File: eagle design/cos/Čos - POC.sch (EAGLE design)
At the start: 117 parts, among them IC1 SQJ952EP-T1_GE3, IC10 LM74670QDGKRQ1, IC11 LM74670QDGKRQ1, IC12 LM74670QDGKRQ1, IC13 MCP73871-2CCI/ML, IC14 MCP2515, IC15 LM74670QDGKRQ1, IC16 LM74670QDGKRQ1, IC17 MCP23S08-E/ML, IC18 MCP2561-2, IC19 AD5160BRJZ5-R2, IC2 SQJ952EP-T1_GE3, IC20 MP3221GJ-P, IC21 SQJ952EP-T1_GE3, IC22 LM74670QDGKRQ1, IC23 SQJ952EP-T1_GE3, IC3 LM74670QDGKRQ1, IC4 SQJ952EP-T1_GE3, IC5 FDMQ8403, IC6 TPS630702RNMT, IC7 LMP92064SD/NOPB, IC8 ATTINY4313-MMH, IC9 PBRC8.00GR50X000

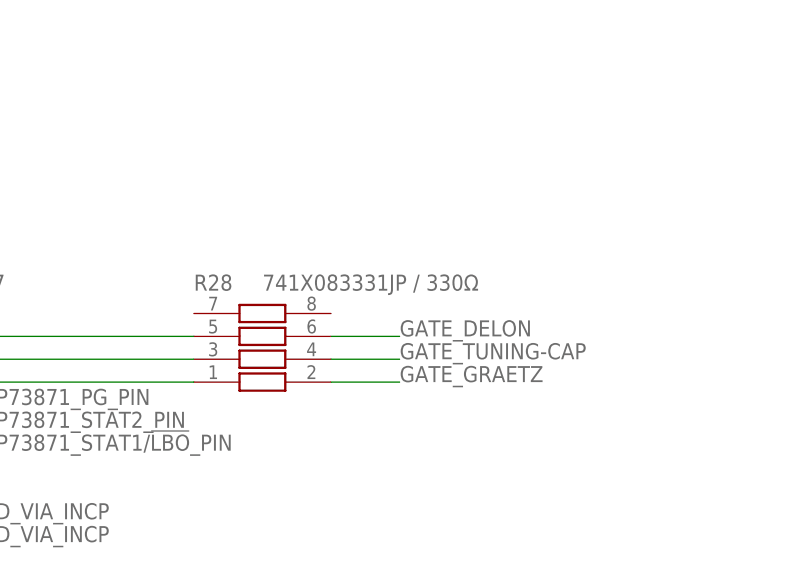
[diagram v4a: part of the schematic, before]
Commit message: - added series resistor for gate pins
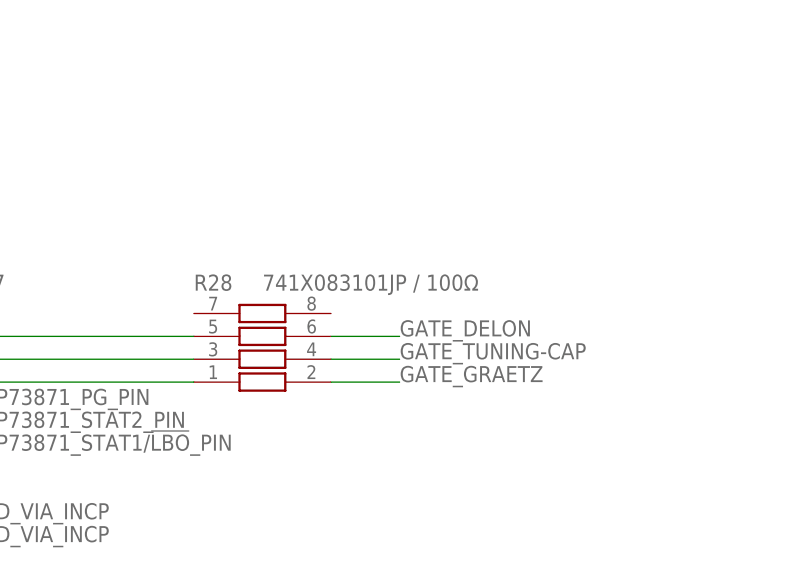
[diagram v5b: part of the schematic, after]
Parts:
- R28: value 741X083331JP / 330Ω -> 741X083101JP / 100Ω
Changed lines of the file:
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@@
 <grid distance="0.1" unitdist="inch" unit="inch" style="lines" multiple="1" display="no" altdistance="0.01" altunitdist="inch" altunit="inch"/>
 <layers>
-<layer number="1" name="Top" color="4" fill="1" visible="yes" active="no"/>
-<layer number="2" name="Route2" color="26" fill="1" visible="yes" active="no"/>
-<layer number="3" name="Route3" color="4" fill="3" visible="yes" active="no"/>
-<layer number="4" name="Route4" color="1" fill="4" visible="yes" active="no"/>
-<layer number="5" name="Route5" color="4" fill="4" visible="yes" active="no"/>
-<layer number="6" name="Route6" color="1" fill="8" visible="yes" active="no"/>
-<layer number="7" name="Route7" color="4" fill="8" visible="yes" active="no"/>
-<layer number="8" name="Route8" color="1" fill="2" visible="yes" active="no"/>
-<layer number="9" name="Route9" color="4" fill="2" visible="yes" active="no"/>
-<layer number="10" name="Route10" color="1" fill="7" visible="yes" active="no"/>
-<layer number="11" name="Route11" color="4" fill="7" visible="yes" active="no"/>
-<layer number="12" name="Route12" color="1" fill="5" visible="yes" active="no"/>
-<layer number="13" name="Route13" color="4" fill="5" visible="yes" active="no"/>
-<layer number="14" name="Route14" color="1" fill="6" visible="yes" active="no"/>
-<layer number="15" name="Route15" color="24" fill="1" visible="yes" active="no"/>
-<layer number="16" name="Bottom" color="1" fill="1" visible="yes" active="no"/>
-<layer number="17" name="Pads" color="2" fill="1" visible="yes" active="no"/>
-<layer number="18" name="Vias" color="2" fill="1" visible="yes" active="no"/>
-<layer number="19" name="Unrouted" color="6" fill="1" visible="yes" active="no"/>
-<layer number="20" name="Dimension" color="24" fill="1" visible="yes" active="no"/>
-<layer number="21" name="tPlace" color="7" fill="1" visible="yes" active="no"/>
-<layer number="22" name="bPlace" color="7" fill="1" visible="yes" active="no"/>
-<layer number="23" name="tOrigins" color="15" fill="1" visible="yes" active="no"/>
-<layer number="24" name="bOrigins" color="15" fill="1" visible="yes" active="no"/>
-<layer number="25" name="tNames" color="7" fill="1" visible="yes" active="no"/>
-<layer number="26" name="bNames" color="7" fill="1" visible="yes" active="no"/>
-<layer number="27" name="tValues" color="7" fill="1" visible="yes" active="no"/>
-<layer number="28" name="bValues" color="7" fill="1" visible="yes" active="no"/>
+<layer number="1" name="Top" color="4" fill="1" visible="no" active="no"/>
+<layer number="2" name="Route2" color="26" fill="1" visible="no" active="no"/>
+<layer number="3" name="Route3" color="4" fill="3" visible="no" active="no"/>
+<layer number="4" name="Route4" color="1" fill="4" visible="no" active="no"/>
+<layer number="5" name="Route5" color="4" fill="4" visible="no" active="no"/>
+<layer number="6" name="Route6" color="1" fill="8" visible="no" active="no"/>
+<layer number="7" name="Route7" color="4" fill="8" visible="no" active="no"/>
+<layer number="8" name="Route8" color="1" fill="2" visible="no" active="no"/>
+<layer number="9" name="Route9" color="4" fill="2" visible="no" active="no"/>
+<layer number="10" name="Route10" color="1" fill="7" visible="no" active="no"/>
+<layer number="11" name="Route11" color="4" fill="7" visible="no" active="no"/>
+<layer number="12" name="Route12" color="1" fill="5" visible="no" active="no"/>
+<layer number="13" name="Route13" color="4" fill="5" visible="no" active="no"/>
+<layer number="14" name="Route14" color="1" fill="6" visible="no" active="no"/>
+<layer number="15" name="Route15" color="24" fill="1" visible="no" active="no"/>
+<layer number="16" name="Bottom" color="1" fill="1" visible="no" active="no"/>
+<layer number="17" name="Pads" color="2" fill="1" visible="no" active="no"/>
+<layer number="18" name="Vias" color="2" fill="1" visible="no" active="no"/>
+<layer number="19" name="Unrouted" color="6" fill="1" visible="no" active="no"/>
+<layer number="20" name="Dimension" color="24" fill="1" visible="no" active="no"/>
+<layer number="21" name="tPlace" color="7" fill="1" visible="no" active="no"/>
+<layer number="22" name="bPlace" color="7" fill="1" visible="no" active="no"/>
+<layer number="23" name="tOrigins" color="15" fill="1" visible="no" active="no"/>
+<layer number="24" name="bOrigins" color="15" fill="1" visible="no" active="no"/>
+<layer number="25" name="tNames" color="7" fill="1" visible="no" active="no"/>
+<layer number="26" name="bNames" color="7" fill="1" visible="no" active="no"/>
+<layer number="27" name="tValues" color="7" fill="1" visible="no" active="no"/>
+<layer number="28" name="bValues" color="7" fill="1" visible="no" active="no"/>
 <layer number="29" name="tStop" color="7" fill="3" visible="no" active="no"/>
 <layer number="30" name="bStop" color="7" fill="6" visible="no" active="no"/>
@@
 <layer number="35" name="tGlue" color="7" fill="4" visible="no" active="no"/>
 <layer number="36" name="bGlue" color="7" fill="5" visible="no" active="no"/>
-<layer number="37" name="tTest" color="7" fill="1" visible="yes" active="no"/>
-<layer number="38" name="bTest" color="7" fill="1" visible="yes" active="no"/>
+<layer number="37" name="tTest" color="7" fill="1" visible="no" active="no"/>
+<layer number="38" name="bTest" color="7" fill="1" visible="no" active="no"/>
 <layer number="39" name="tKeepout" color="4" fill="11" visible="no" active="no"/>
 <layer number="40" name="bKeepout" color="1" fill="11" visible="no" active="no"/>
@@
 <layer number="44" name="Drills" color="7" fill="1" visible="no" active="no"/>
 <layer number="45" name="Holes" color="7" fill="1" visible="no" active="no"/>
-<layer number="46" name="Milling" color="3" fill="1" visible="yes" active="no"/>
-<layer number="47" name="Measures" color="7" fill="1" visible="yes" active="no"/>
-<layer number="48" name="Document" color="7" fill="1" visible="yes" active="no"/>
-<layer number="49" name="Reference" color="7" fill="1" visible="yes" active="no"/>
-<layer number="50" name="dxf" color="7" fill="1" visible="yes" active="no"/>
-<layer number="51" name="tDocu" color="7" fill="1" visible="yes" active="no"/>
-<layer number="52" name="bDocu" color="7" fill="1" visible="yes" active="no"/>
-<layer number="53" name="tGND_GNDA" color="7" fill="9" visible="yes" active="no"/>
-<layer number="54" name="bGND_GNDA" color="1" fill="9" visible="yes" active="no"/>
-<layer number="56" name="wert" color="7" fill="1" visible="yes" active="no"/>
-<layer number="57" name="tCAD" color="7" fill="1" visible="yes" active="no"/>
-<layer number="59" name="tCarbon" color="7" fill="1" visible="yes" active="no"/>
-<layer number="60" name="bCarbon" color="7" fill="1" visible="yes" active="no"/>
+<layer number="46" name="Milling" color="3" fill="1" visible="no" active="no"/>
+<layer number="47" name="Measures" color="7" fill="1" visible="no" active="no"/>
+<layer number="48" name="Document" color="7" fill="1" visible="no" active="no"/>
+<layer number="49" name="Reference" color="7" fill="1" visible="no" active="no"/>
+<layer number="50" name="dxf" color="7" fill="1" visible="no" active="no"/>
+<layer number="51" name="tDocu" color="7" fill="1" visible="no" active="no"/>
+<layer number="52" name="bDocu" color="7" fill="1" visible="no" active="no"/>
+<layer number="53" name="tGND_GNDA" color="7" fill="9" visible="no" active="no"/>
+<layer number="54" name="bGND_GNDA" color="1" fill="9" visible="no" active="no"/>
+<layer number="56" name="wert" color="7" fill="1" visible="no" active="no"/>
+<layer number="57" name="tCAD" color="7" fill="1" visible="no" active="no"/>
+<layer number="59" name="tCarbon" color="7" fill="1" visible="no" active="no"/>
+<layer number="60" name="bCarbon" color="7" fill="1" visible="no" active="no"/>
 <layer number="88" name="SimResults" color="9" fill="1" visible="yes" active="yes"/>
 <layer number="89" name="SimProbes" color="9" fill="1" visible="yes" active="yes"/>
@@
 <part name="FD2" library="Fiducial" deviceset="FID" device="_40MIL"/>
 <part name="FD3" library="Fiducial" deviceset="FID" device="_40MIL"/>
-<part name="R28" library="741X083331JP Resistor Array" deviceset="741X083331JP" device="" value="741X083331JP / 330Ω"/>
+<part name="R28" library="741X083331JP Resistor Array" deviceset="741X083331JP" device="" value="741X083101JP  / 100Ω"/>
 </parts>
 <sheets>

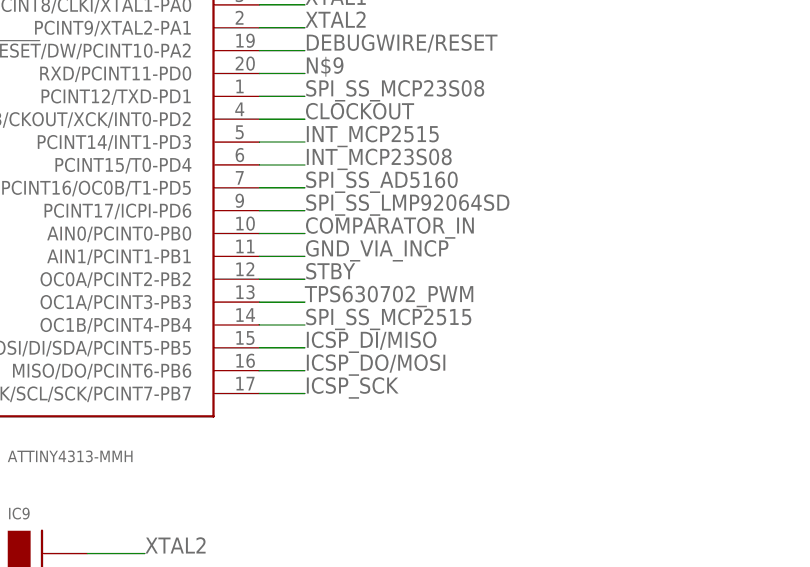
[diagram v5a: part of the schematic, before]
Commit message: in sch and brd: - pin swapped STBY and buck-boost PWM pins so that the comparator can work with timer1; buck-boost PWM is only 8bit
in cos.c and .h:
- configured comparator pins
- configured comparator to trigger on rising edge and enabled timer1 input capture function,
- configured timer1 for input capture, noise canceler, capture on rising edge, TOP = ICR1
- configured ICIE1 (Input Capture) and TOIE1 (timer overflow) interrupts
- enabled pin change interrupts for INT_MCP23S08_pin - PD4,
- wrote skeleton TIMER1_CAPT_vect and TIMER1_OVF_vect ISRs
- OCR_BUCK_BOOST holds PWM for Buck/Boost regulator
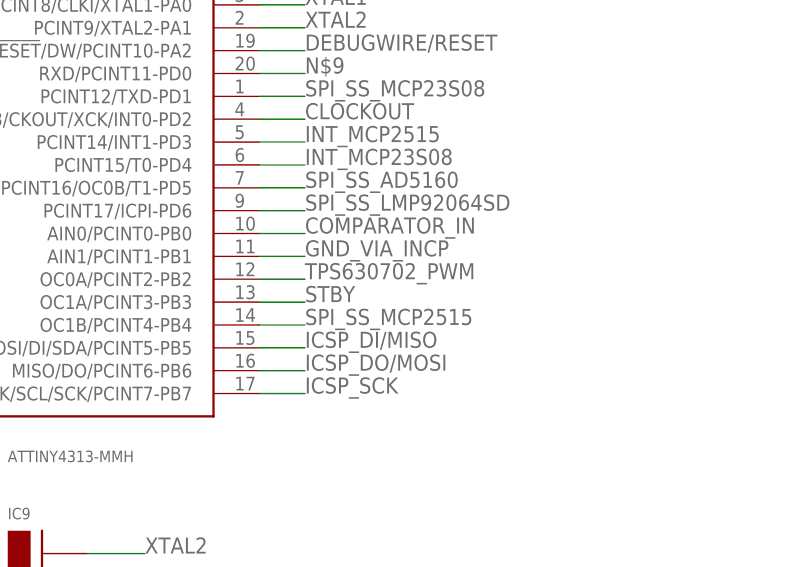
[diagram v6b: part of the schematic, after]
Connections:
- net STBY: now also IC8.OC1A/PCINT3-PB3; no longer IC8.OC0A/PCINT2-PB2
- net TPS630702_PWM: now also IC8.OC0A/PCINT2-PB2; no longer IC8.OC1A/PCINT3-PB3
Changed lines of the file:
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@@
 <?xml version="1.0" encoding="utf-8"?>
 <!DOCTYPE eagle SYSTEM "eagle.dtd">
-<eagle version="9.4.2">
+<eagle version="9.4.0">
 <drawing>
 <settings>
@@
 </segment>
 <segment>
-<pinref part="IC8" gate="G$1" pin="OC0A/PCINT2-PB2"/>
-<wire x1="190.5" y1="134.62" x2="195.58" y2="134.62" width="0.1524" layer="91"/>
-<label x="195.58" y="134.62" size="1.778" layer="95"/>
+<pinref part="IC8" gate="G$1" pin="OC1A/PCINT3-PB3"/>
+<wire x1="190.5" y1="132.08" x2="195.58" y2="132.08" width="0.1524" layer="91"/>
+<label x="195.58" y="132.08" size="1.778" layer="95"/>
 </segment>
 </net>
@@
 </segment>
 <segment>
-<pinref part="IC8" gate="G$1" pin="OC1A/PCINT3-PB3"/>
-<wire x1="190.5" y1="132.08" x2="195.58" y2="132.08" width="0.1524" layer="91"/>
-<label x="195.58" y="132.08" size="1.778" layer="95"/>
-</segment>
-</net>
+<pinref part="IC8" gate="G$1" pin="OC0A/PCINT2-PB2"/>
+<wire x1="190.5" y1="134.62" x2="195.58" y2="134.62" width="0.1524" layer="91"/>
+<label x="195.58" y="134.62" size="1.778" layer="95"/>
+</segment>
+</net>

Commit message: brd & sch: routing cleanup, small library changes
in cos.c: fiddling around with voltage and current variables
in lmp92064sd: small #define changes
in mcp23s08: first steps in driver dev.
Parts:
- added LI-: Li-Ion Cell +, testpad:TPSQPAD1-13
- C10: value 0.1μF -> 1μF
- C11: value 10pF -> 100nF
- C13: value 10pF -> 10μF; device rcl:C-EUC0402 -> rcl:C-EUC0603
- C14: value 0.1μF -> 10pF
- C15: value 100nF -> 0.1μF
- C16: value 0.1μF -> 4.7μF
- C17: value 10μF -> 10pF; device rcl:C-EUC0603 -> rcl:C-EUC0402
- C18: value 4.7μF -> 0.1μF
- C9: value 1μF -> 0.1μF
- IC10: value LM74670QDGKRQ1 -> LMP92064SD/NOPB; device LM74670 - Smart Diode Rectifier Controller:LM74670 -> LMP92064SD - LMP92064 Precision Low-Side, 125-kSps Simultaneous Sampling Current Sensor and Voltage Monitor With SPI:LM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
- IC7: value LMP92064SD/NOPB -> ATTINY4313-MMH; device LMP92064SD - LMP92064 Precision Low-Side, 125-kSps Simultaneous Sampling Current Sensor and Voltage Monitor With SPI:LM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 -> ATtiny4313 microcontroller:ATTINY4313VQFN-20; SPICEPREFIX (none) -> X
- IC8: value ATTINY4313-MMH -> PBRC8.00GR50X000; device ATtiny4313 microcontroller:ATTINY4313VQFN-20 -> PRQV8.00CR1510Y00L - 8MHz resonator:PRQV; SPICEPREFIX X -> (none)
- IC9: value PBRC8.00GR50X000 -> LM74670QDGKRQ1; device PRQV8.00CR1510Y00L - 8MHz resonator:PRQV -> LM74670 - Smart Diode Rectifier Controller:LM74670
- R10: value 110k -> 47k
- R11: value 10k -> 47k
- R13, R4: value 47k -> 100k
- R14: value 47k -> 320k
- R2: value 43mR, 200mW -> 22k; device rcl:R-EU_R2512 -> rcl:R-EU_R0402
- R25: value 653k -> 741X083101JP / 100Ω; device rcl:R-EU_R0402 -> 741X083331JP Resistor Array:741X083331JP
- R26: value 100k -> 653k
- R27: value 120 -> 100k
- R28: value 741X083101JP / 100Ω -> 120; device 741X083331JP Resistor Array:741X083331JP -> rcl:R-EU_R0402
- R3: value 22k -> 47k
- R5: value 100k -> 43mR, 200mW; device rcl:R-EU_R0402 -> rcl:R-EU_R2512
- R7: value 320k -> 337k
- R8: value 100k -> 110k
- R9: value 337k -> 10k
- renumbered CONN1 to ICSP, CONN2 to L, CONN3 to H, TP1 to DYNAMO2, TP2 to DYNAMO1, TP7 to LI+
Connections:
- net 5V0_TP-IN: now also C13.1; no longer C17.1
- net 5V0_TP-OUT: now also C15.1, C17.1, C18.1, C9.1, IC10.VDD_8, IC10.VDIG_9, IC7.VCC, R10.2, R11.2; no longer C10.1, C11.1, C12.1, C13.1, IC7.VDD_8, IC7.VDIG_9, IC8.VCC, R13.2, R9.2
- net 6V0_TP-IN: now also R26.2; no longer R25.2
- net CANH: now also R28.2; no longer R27.2
- net CANL: now also R28.1; no longer R27.1
- net CLOCKOUT: now also IC7.PCINT13/CKOUT/XCK/INT0-PD2; no longer IC8.PCINT13/CKOUT/XCK/INT0-PD2
- net COMPARATOR_IN: now also IC7.AIN0/PCINT0-PB0, R4.2; no longer IC8.AIN0/PCINT0-PB0, R5.2
- net D2_VCAPH: now also C12.2, IC9.VCAPH; no longer C16.2, IC10.VCAPH
- net D2_VCAPL: now also C12.1, IC9.VCAPL; no longer C16.1, IC10.VCAPL
- net DEBUGWIRE/RESET: now also IC7.!RESET!/DW/PCINT10-PA2; no longer IC8.!RESET!/DW/PCINT10-PA2
- net DYNAMO_2_AFTER_SW: now also IC9.CATHODE; no longer IC10.CATHODE
- net FB: now also R26.1, R27.2; no longer R25.1, R26.2
- net GATE_D2: now also IC9.GATE, IC9.GATE_PULLD; no longer IC10.GATE, IC10.GATE_PULLD
- net GATE_DELON: now also R25.6, R9.2; no longer R11.2, R28.6
- net GATE_GRAETZ: now also R25.2; no longer R28.2
- net GATE_TUNING-CAP: now also R25.4; no longer R28.4
- net GND: now also IC9.ANODE, R15.1, R2.1, R9.1; no longer IC10.ANODE, R11.1, R3.1
- net GND_VIA_INCP: now also C16.2, IC10.10_DGND, IC10.2_REFG, IC10.3_INCP, IC10.6_INVG, IC10.7_GND, IC10.RESET_16, IC7.AIN1/PCINT1-PB1, IC7.GND, LI-.TP, R13.1, R27.1, R5.2; no longer C12.2, IC7.10_DGND, IC7.2_REFG, IC7.3_INCP, IC7.6_INVG, IC7.7_GND, IC7.RESET_16, IC8.AIN1/PCINT1-PB1, IC9.GND, R10.1, R15.1, R2.2, R26.1
- net ICSP_DI/MISO: now also IC7.MOSI/DI/SDA/PCINT5-PB5; no longer IC8.MOSI/DI/SDA/PCINT5-PB5
- net ICSP_DO/MOSI: now also IC7.MISO/DO/PCINT6-PB6; no longer IC8.MISO/DO/PCINT6-PB6
- net ICSP_SCK: now also IC7.USCK/SCL/SCK/PCINT7-PB7; no longer IC8.USCK/SCL/SCK/PCINT7-PB7
- net INCN: now also IC10.4_INCN, R5.1; no longer IC7.4_INCN, R2.1
- net INT_MCP23S08: now also IC7.PCINT15/T0-PD4; no longer IC8.PCINT15/T0-PD4
- net INT_MCP2515: now also IC7.PCINT14/INT1-PD3; no longer IC8.PCINT14/INT1-PD3
- net INVP: now also IC10.5_INVP, R14.1, R15.2; no longer IC7.5_INVP, R7.1, R8.2
- net MCP73871_PG_PIN: now also R10.1; no longer R12.1
- net MCP73871_STAT1/!LBO!_PIN: now also R11.1; no longer R13.1
- net MCP73871_STAT2_PIN: now also R12.1; no longer R14.1
- net N$10: now also R25.3; no longer R28.3
- net N$11: now also R25.1; no longer R28.1
- net N$17: now also C10.1, IC10.REFC_1; no longer C9.1, IC7.REFC_1
- net N$4: now also R2.2, R4.1; no longer R3.2, R5.1
- net N$6: now also R25.5; no longer R28.5
- net N$9: now also IC7.RXD/PCINT11-PD0; no longer IC8.RXD/PCINT11-PD0
- net PROG3: now also R13.2; no longer R15.2
- net SOLAR-CELL_TP-IN: now also TP5_IN.TP; no longer TP5_OUT.TP
- net SOLAR-CELL_TP-OUT: now also TP5_OUT.TP; no longer TP5_IN.TP
- net SPI_MISO: now also IC10.SDO_11; no longer IC7.SDO_11
- net SPI_MOSI: now also IC10.SDI_12; no longer IC7.SDI_12
- net SPI_SCK: now also IC10.SCLK_13; no longer IC7.SCLK_13
- net SPI_SS_AD5160: now also IC7.PCINT16/OC0B/T1-PD5; no longer IC8.PCINT16/OC0B/T1-PD5
- net SPI_SS_LMP92064SD: now also IC10.CSB_14, IC7.PCINT17/ICPI-PD6; no longer IC7.CSB_14, IC8.PCINT17/ICPI-PD6
- net SPI_SS_MCP23S08: now also IC7.PCINT12/TXD-PD1; no longer IC8.PCINT12/TXD-PD1
- net SPI_SS_MCP2515: now also IC7.OC1B/PCINT4-PB4; no longer IC8.OC1B/PCINT4-PB4
- net STBY: now also IC7.OC1A/PCINT3-PB3; no longer IC8.OC1A/PCINT3-PB3
- net TPS630702_PWM: now also IC7.OC0A/PCINT2-PB2; no longer IC8.OC0A/PCINT2-PB2
- net TUNIN_CAP2_BIAS: now also R3.1; no longer R4.1
- net VAUX: now also C11.1; no longer C15.1
- net VPCC: now also R7.1, R8.2; no longer R10.2, R9.1
- net V_DC_TP-IN: now also R3.2; no longer R4.2
- net V_LI-ION_BATTERY-CELL: now also C16.1; no longer C18.1
- net XTAL1: now also IC7.PCINT8/CLKI/XTAL1-PA0, IC8.XTAL1; no longer IC8.PCINT8/CLKI/XTAL1-PA0, IC9.XTAL1
- net XTAL2: now also IC7.PCINT9/XTAL2-PA1, IC8.XTAL2; no longer IC8.PCINT9/XTAL2-PA1, IC9.XTAL2
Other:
- note added: "LMP92064SD Voltage/Current measurement"
- note added: "SPI"
- note removed: "TODO: shunt?"
- moved on the sheet: C10, C11, C12, C13, C14, C15, C16, C17, C18, C9, R10, R11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

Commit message: čos rev.1 complete - added BOM, slight update to library - routed 6V0 Boost converter enable pin to microcontroller: MP3221_EN_pin - updated cos.c and .h with new MP3221_EN_pin instructions
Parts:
- removed R28: 120, rcl:R-EU_R0402
- added C36: 0.1μF, rcl:C-EUC0402
- added Q1: SI2399DS-T1-GE3, Transistor:BSS84
- C11: value 100nF -> 0.1μF
- C19, C20, C22: value 10μF -> 22μF
- C23: value 5600μF -> 4700μF
- C33: value 0.1μF -> 3.3nF
- C34: value 22μF -> 0.1μF
- C35: value 0.1μF -> 22μF; device rcl:C-EUC0402 -> rcl:C-EUC0805
- IC6: value TPS630702RNMT -> TPS630701RNMT
- L1: value XFL4020-152MEC -> XFL4020-152MEC - 1.5uH
- L2: value DJNR6045-100-S -> SRN6045-2R2Y - 2.2μH
- R14: value 320k -> 324k
- R24: value 100k -> 10k
- R26: value 653k -> 536k
- R7: value 337k -> 340k
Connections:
- removed net EN2: IC20.4_EN, R24.1
- removed net N$9: IC7.RXD/PCINT11-PD0
- new net MP3221_EN: IC20.4_EN, IC7.RXD/PCINT11-PD0, R24.1
- new net MP3221_FAULT: C33.2, IC20.6_FAULT, Q1.G
- new net N$2: L2.1, Q1.D
- net 5V0_TP-OUT: now also C34.1; no longer C33.1
- net 6V0_TP-IN: now also C35.1; no longer C34.1
- net CANH: no longer R28.2
- net CANL: no longer R28.1
- net D_VLIION_VCAPH1: now also C36.2; no longer C35.2
- net D_VLIION_VCAPL1: now also C36.1; no longer C35.1
- net GND_VIA_INCP: now also C35.2, R24.2; no longer C33.2
- net V_LI-ION_OUT: now also C33.1, Q1.S; no longer L2.1, R24.2
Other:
- note added: "647-UHD1V471MPD - 470uF/35V 647-UHD1V331MPD - 330uF/35V 647-UHD1V221MPD6 - 220uF/35V 647-UHV1V151MPD - 150uF/35V"
- note removed: "TODO - enable via microcontroller?"
- moved on the sheet: C33, C34, C35, L2, R24
